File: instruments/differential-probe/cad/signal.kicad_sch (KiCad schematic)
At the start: 27 parts, among them J3 BNC / panel / 50 R, Q1 MMBT3906,215, SW1 DPDT / ON-ON, U3 ADA4817-1ARDZ-R7, U4 OPA810IDR, U5 TLV1704AIPWR, U6 TLV1702AIDGKR, U7 CD4013BM96

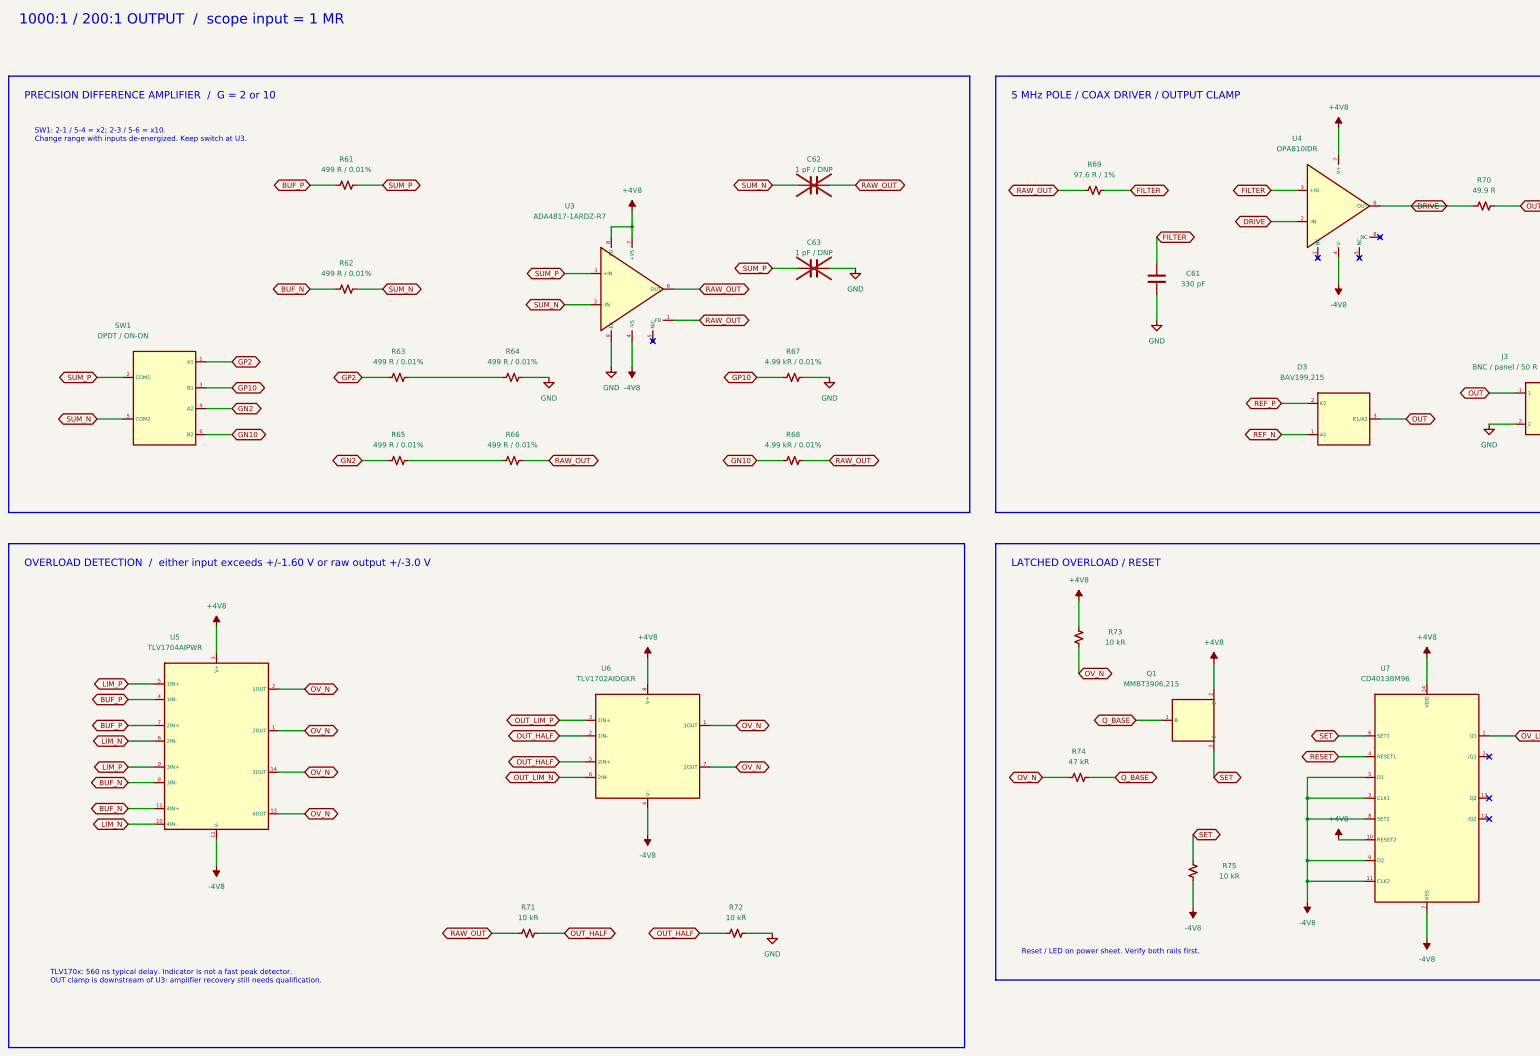
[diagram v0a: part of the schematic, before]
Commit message: fix(instruments): compact the probe and keep range switching outside feedback
Add fine compensation trimmers, fixed OPA810 gain stages and conservative
initial-envelope warning thresholds with analog-offset allowances. Reduce
the PCB to 240 x 84 mm using the simultaneous 3 kV input envelope, retaining
matched divider geometry, slots and explicit spacing rules.

Regenerate native schematic, BOM, routed PCB and validation artifacts.
Document manufacturer-model limits, bench qualification and the corrected
stage-53 CT calculations without changing the pinned power-stage board.
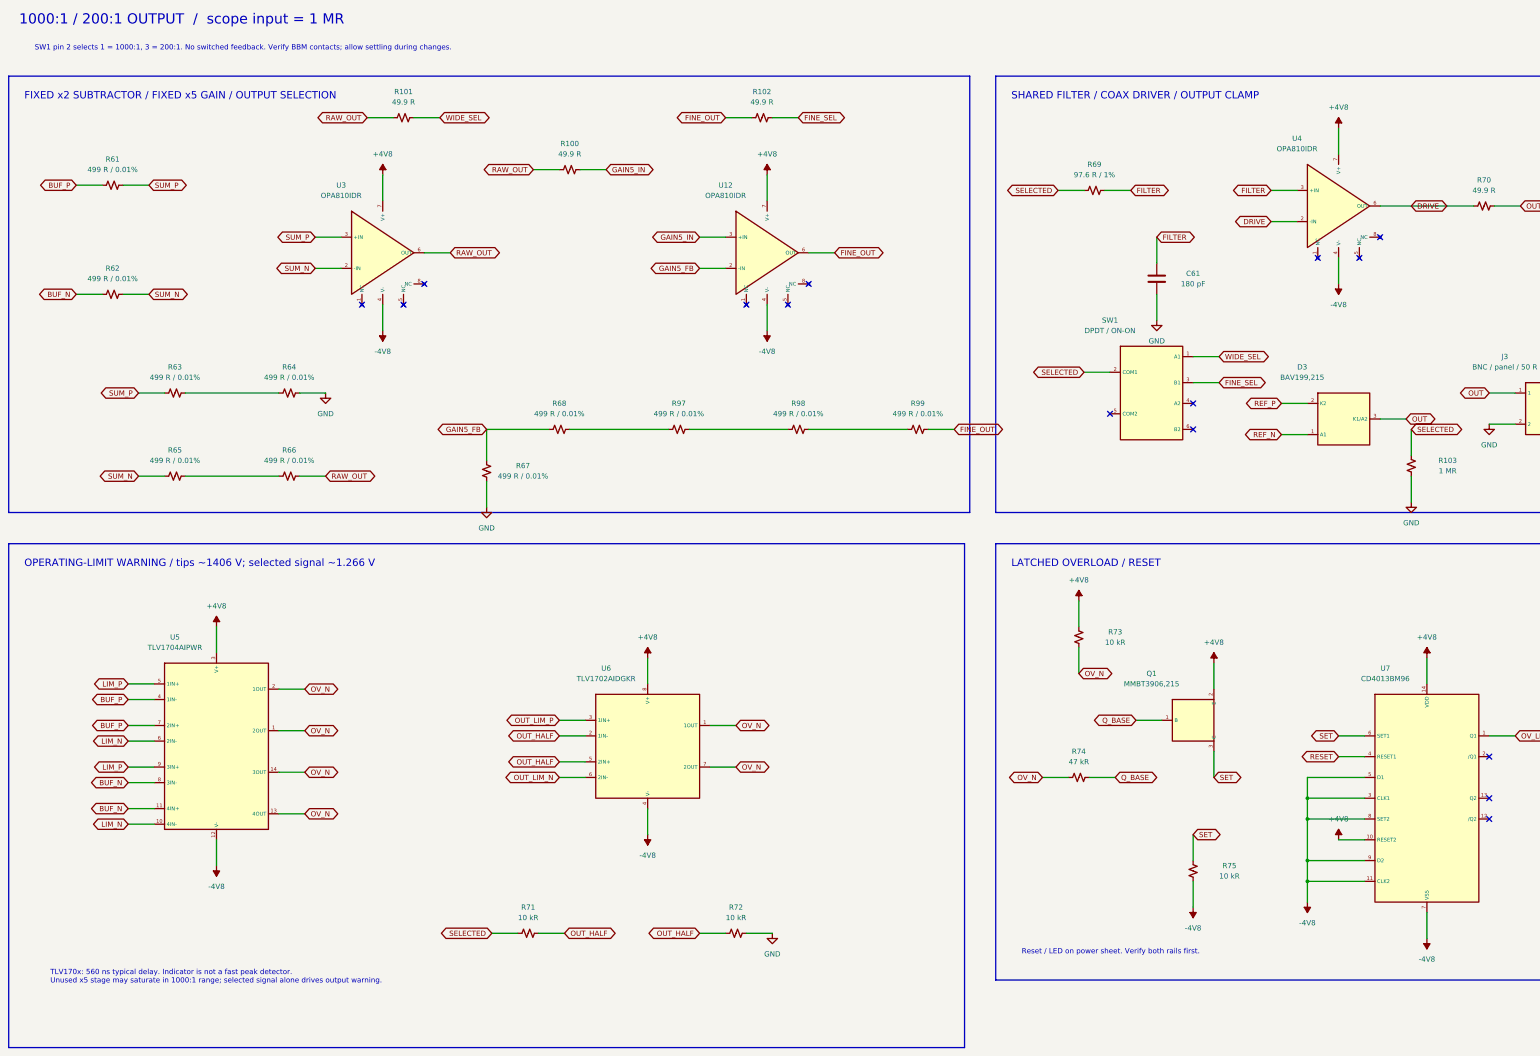
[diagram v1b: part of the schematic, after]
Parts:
- removed C62, C63: 1 pF / DNP, Capacitor_SMD:C_0805_2012Metric, symbol Probe:C
- added R100, R101, R102: 49.9 R, Resistor_SMD:R_0805_2012Metric, symbol Probe:R_Small_US
- added R103: 1 MR, Resistor_SMD:R_0805_2012Metric, symbol Probe:R_Small_US
- added R97, R98, R99: 499 R / 0.01%, Resistor_SMD:R_0603_1608Metric, symbol Probe:R_Small_US
- added U12: OPA810IDR, Package_SO:SOIC-8_3.9x4.9mm_P1.27mm, symbol Probe:OPA810
- C61: value 330 pF -> 180 pF; MPN C0805C331J5GACTU -> C0805C181J5GACTU
- R67, R68: value 4.99 kR / 0.01% -> 499 R / 0.01%; LCSC C3942722 -> (none); MPN RNCF0603TKY4K99 -> RNCF0603TKY499R
- U3: value ADA4817-1ARDZ-R7 -> OPA810IDR; footprint Probe:ADA4817_RD-8-4 -> Package_SO:SOIC-8_3.9x4.9mm_P1.27mm; symbol Probe:ADA4817 -> Probe:OPA810; LCSC C207502 -> C1852077; MPN ADA4817-1ARDZ-R7 -> OPA810IDR; Manufacturer Analog Devices -> Texas Instruments
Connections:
- net +4V8: now also U12.7 (V+); no longer U3.8 (PD)
- net -4V8: now also U12.4 (V-)
- net GND: now also R103.2; no longer U3.9 (EP)
- net RAW_OUT: now also R100.1, R101.1; no longer R68.2, R69.1, R71.1, U3.1 (FB)
- net SUM_N: now also R65.1; no longer SW1.5 (COM2)
- net SUM_P: now also R63.1; no longer SW1.2 (COM1)
- net GN10: no longer names the net of SW1.6 (B2)
- net GN10: no longer R68.1
- net GN2: no longer names the net of SW1.4 (A2)
- net GN2: no longer R65.1
- net GP10 renamed FINE_SEL
- net FINE_SEL: now also R102.2; no longer R67.1
- net GP2 renamed WIDE_SEL
- net WIDE_SEL: now also R101.2; no longer R63.1
- new net: R68.2, R97.1
- new net: R97.2, R98.1
- new net: R98.2, R99.1
- new net FINE_OUT: R102.1, R99.2, U12.6 (OUT)
- new net GAIN5_FB: R67.1, R68.1, U12.2 (-IN)
- new net GAIN5_IN: R100.2, U12.3 (+IN)
- new net SELECTED: R103.1, R69.1, R71.1, SW1.2 (COM1)
- no-connect marks 7 -> 15
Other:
- note added: "FIXED x2 SUBTRACTOR / FIXED x5 GAIN / OUTPUT SELECTION"
- note added: "OPERATING-LIMIT WARNING / tips ~1406 V; selected signal ~1.266 V"
- note added: "SHARED FILTER / COAX DRIVER / OUTPUT CLAMP"
- note added: "SW1 pin 2 selects 1 = 1000:1, 3 = 200:1. No switched feedback. Verify BBM contacts; allow settling during changes."
- note added: "TLV170x: 560 ns typical delay. Indicator is not a fast peak detector. Unused x5 stage may saturate in 1000:1 range; selected signal alone drives output warning."
- note removed: "5 MHz POLE / COAX DRIVER / OUTPUT CLAMP"
- note removed: "OVERLOAD DETECTION / either input exceeds +/-1.60 V or raw output +/-3.0 V"
- note removed: "PRECISION DIFFERENCE AMPLIFIER / G = 2 or 10"
- note removed: "SW1: 2-1 / 5-4 = x2; 2-3 / 5-6 = x10. Change range with inputs de-energized. Keep switch at U3."
- note removed: "TLV170x: 560 ns typical delay. Indicator is not a fast peak detector. OUT clamp is downstream of U3: amplifier recovery still needs qualification."
- moved on the sheet: R61, R62, R63, R64, R65, R66, R67, R68, SW1
